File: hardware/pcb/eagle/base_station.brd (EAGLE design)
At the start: 100 x 112 mm, 105 parts, among them CON1 RJ45-8PTH, CON2 RJ45-8PTH, CON3 RJ45-8PTH, CON4 RJ45-8PTH, CON5 RJ45-8PTH, CON6 RJ45-8PTH, CON7 RJ45-8PTH, CON8 RJ45-8PTH, IC1 LTC2851S, IC10 LTC2851S, IC11 LTC2851S, IC12 LTC2851S, IC13 LTC2851S, IC14 LTC2851S, IC15 LTC2851S, IC16 LTC2851S, IC17 NC7WZ16P6X, IC18 7Q-16.368MBG-T, IC19 LTC2851S, IC2 LTC2851S, IC20 LTC2851S, IC21 LTC2851S, IC22 LTC2851S, IC23 LTC2851S, IC24 LTC2851S, IC25 LTC2851S, IC26 LTC2851S, IC3 LTC2851S, IC4 LTC2851S, IC5 LTC2851S, IC6 LTC2851S, IC7 LTC2851S, IC8 LTC2851S, IC9 LTC2851S

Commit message: Changes to oscillator circuit. Added RJ45 for SPI
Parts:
- removed R31: 100k, rcl:R0603
- added CON12: RJ45-8PTH, SparkFun:RJ45-8
- added U$3: WING4, Papilio:WINGSIDE_4BIT
- moved IC17 0.25 mm to (52.8, 39.4)
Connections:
- net N$1 renamed CLK_FPGA
- removed net NC: U$1.A25
- new net MISO: CON12.4, U$3.2
- new net MOSI: CON12.6, U$3.3
- new net N/C: IC17.P$1
- new net SCLK: CON12.8, U$3.4
- new net SS: CON12.3, U$3.1
- new net START: CON12.2, U$1.A25
- net +24V_L: now also CON12.1
- net CLK_OUT: no longer R31.1
- net GND: now also CON12.5, CON12.7
- net N$6: no longer IC17.P$1, R31.2
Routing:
- net +24V_L: track 84.6 -> 133.9 mm
- net CLK_OUT_2: track 44.2 -> 31.4 mm
- net START: track 0.00 -> 9.98 mm, vias 0 -> 1
- net SS: track 0.00 -> 9.46 mm, vias 0 -> 1
- net SCLK: track 0.00 -> 6.39 mm, vias 0 -> 1
- net MOSI: track 0.00 -> 6.39 mm, vias 0 -> 1
- net MISO: track 0.00 -> 6.39 mm, vias 0 -> 1
- net N$6: track 13.9 -> 9.89 mm
- net CLK_OUT: track 169.7 -> 169.1 mm
- net VCC: vias 35 -> 34
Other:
- board size 100 x 112 mm -> 105 x 112 mm

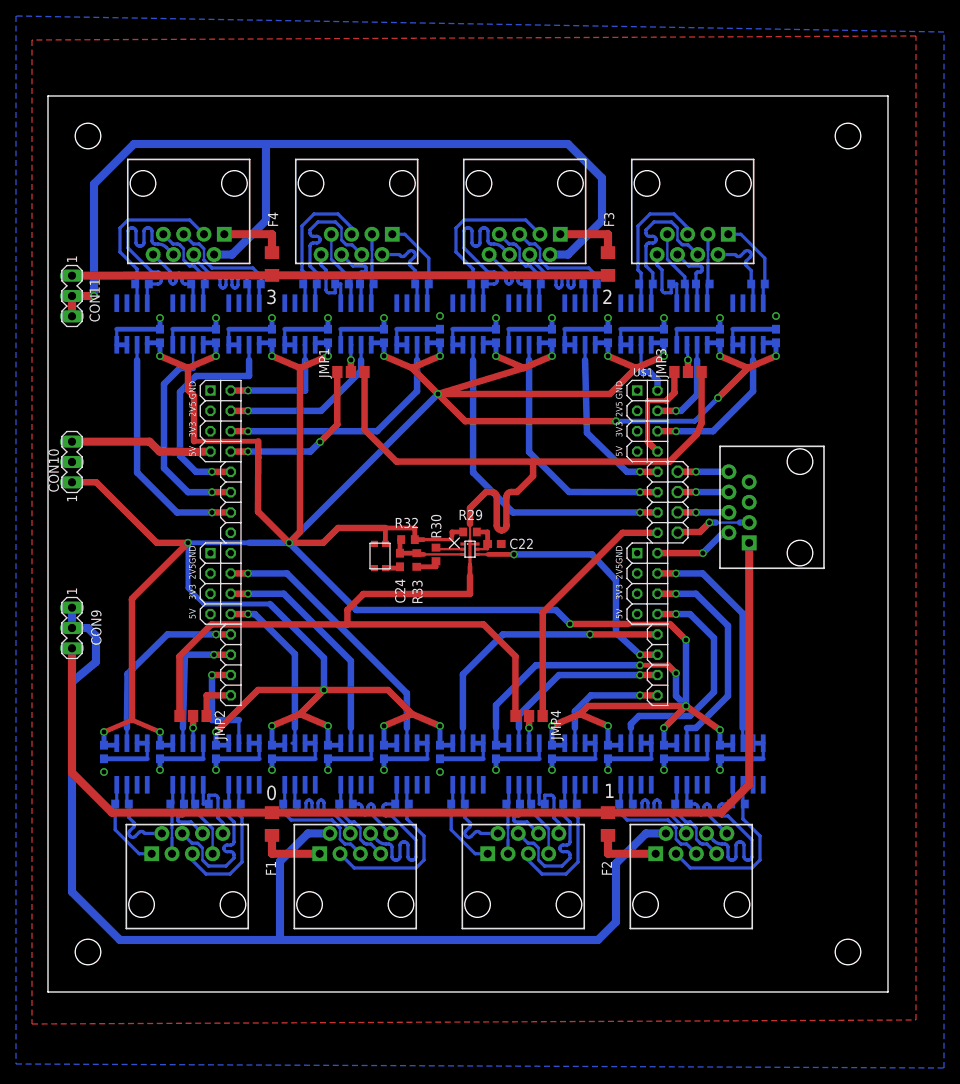
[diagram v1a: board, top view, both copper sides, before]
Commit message: Added silk screen layers, and ammended component names to suit
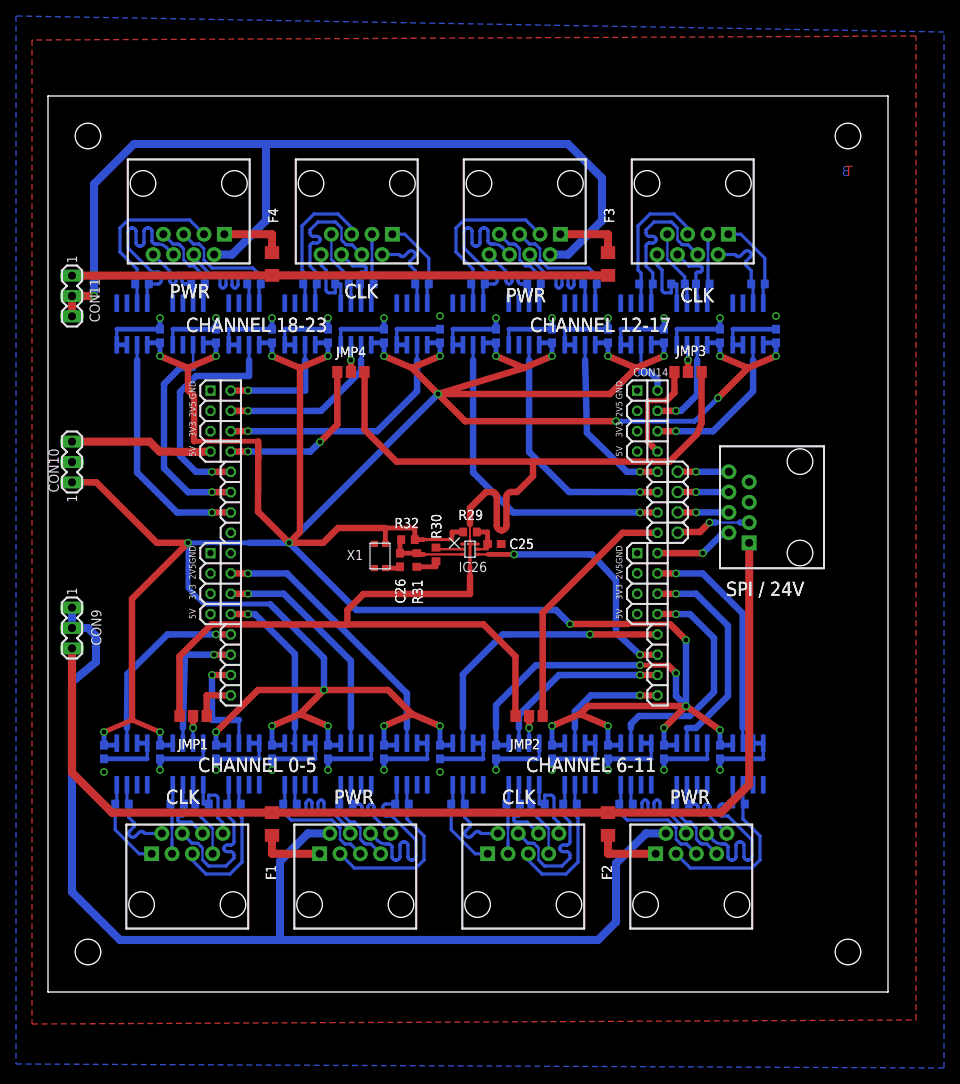
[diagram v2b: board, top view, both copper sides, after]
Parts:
- removed IC25: LTC2851S, texas_lvds:SOIC8
- added X1: 7Q-16.368MBG-T, texas_lvds:4-SMD
- C24: value 2200p -> 0.1uF
- C26: value 0.1uF -> 2200p
- IC17: value NC7WZ16P6X -> LTC2851S; device texas_lvds:NC7WZ16P6X -> texas_lvds:SOIC8
- IC18: value 7Q-16.368MBG-T -> LTC2851S; device texas_lvds:4-SMD -> texas_lvds:SOIC8
- IC26: value LTC2851S -> NC7WZ16P6X; device texas_lvds:SOIC8 -> texas_lvds:NC7WZ16P6X
- moved JMP4 48.4 mm to (37.9, 61.5), turned to 90 degrees
- moved JMP1 47.3 mm to (18.1, 18.5), turned to 270 degrees
- moved C25 43.4 mm to (55.8, 40.0), flipped to the top, turned to 0 degrees
- moved JMP2 42.0 mm to (60.1, 18.5)
- moved C24 41.0 mm to (14.0, 66.0), flipped to the bottom
- moved IC26 39.9 mm to (52.8, 39.4), flipped to the top, turned to 270 degrees
- moved C22 38.1 mm to (28.0, 66.0), flipped to the bottom, turned to 90 degrees
- moved C26 32.2 mm to (44.0, 38.0), flipped to the top
- moved IC18 31.0 mm to (52.5, 67.5), flipped to the bottom, turned to 0 degrees
- moved IC17 28.9 mm to (59.5, 67.5), flipped to the bottom, turned to 0 degrees
- moved IC20 28.0 mm to (38.5, 67.5)
- moved IC23 28.0 mm to (17.5, 67.5)
- moved C10 14.0 mm to (70.0, 14.0)
- moved C12 14.0 mm to (84.0, 14.0)
- moved C13 14.0 mm to (91.0, 66.0)
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- renumbered R33 to R31, U$1 to CON14, U$3 to CON13
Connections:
- net CLK_1: now also JMP1.2; no longer JMP2.2
- net CLK_2: now also JMP2.2; no longer JMP4.2
- net CLK_4: now also IC20.3, JMP4.2; no longer IC22.3, JMP1.2
- net CLK_FPGA: now also IC26.P$4; no longer IC17.P$4
- net CLK_INV_2: now also R10.2; no longer R9.2
- net CLK_INV_3: now also R17.2; no longer R16.2
- net CLK_INV_4: now also IC20.6, R24.2; no longer IC22.6, R23.2
- net CLK_NINV_2: now also R10.1; no longer R9.1
- net CLK_NINV_3: now also R17.1; no longer R16.1
- net CLK_NINV_4: now also IC20.5, R24.1; no longer IC22.5, R23.1
- net CLK_OUT: now also IC26.P$6; no longer IC17.P$6
- net CLK_OUT_1: now also JMP1.1; no longer JMP2.1
- net CLK_OUT_2: now also JMP2.1; no longer JMP4.1
- net CLK_OUT_4: now also JMP4.1; no longer JMP1.1
- net DT_1_4: now also IC20.2; no longer IC22.2
- net DT_1_INV_2: now also R9.1; no longer R10.1
- net DT_1_INV_3: now also R16.1; no longer R17.1
- net DT_1_INV_4: now also IC20.8, R23.1; no longer IC22.8, R24.1
- net DT_1_NINV_2: now also R9.2; no longer R10.2
- net DT_1_NINV_3: now also R16.2; no longer R17.2
- net DT_1_NINV_4: now also IC20.7, R23.2; no longer IC22.7, R24.2
- net DT_2_2: now also IC9.2; no longer IC7.2
- net DT_2_3: now also IC15.2; no longer IC13.2
- net DT_2_INV_2: now also IC9.7, R11.1; no longer IC7.7, R8.1
- net DT_2_INV_3: now also IC15.7, R18.1; no longer IC13.7, R15.1
- net DT_2_INV_4: now also R25.1; no longer R22.1
- net DT_2_NINV_2: now also IC9.8, R11.2; no longer IC7.8, R8.2
- net DT_2_NINV_3: now also IC15.8, R18.2; no longer IC13.8, R15.2
- net DT_2_NINV_4: now also R25.2; no longer R22.2
- net DT_3_2: now also IC7.2; no longer IC9.2
- net DT_3_3: now also IC13.2; no longer IC15.2
- net DT_3_4: now also IC19.2; no longer IC23.2
- net DT_3_INV_2: now also IC7.7, R8.1; no longer IC9.7, R11.1
- net DT_3_INV_3: now also IC13.7, R15.1; no longer IC15.7, R18.1
- net DT_3_INV_4: now also IC19.7, R22.1; no longer IC23.7, R25.1
- net DT_3_NINV_2: now also IC7.8, R8.2; no longer IC9.8, R11.2
- net DT_3_NINV_3: now also IC13.8, R15.2; no longer IC15.8, R18.2
- net DT_3_NINV_4: now also IC19.8, R22.2; no longer IC23.8, R25.2
- net DT_4_3: now also IC17.2; no longer IC19.2
- net DT_4_4: now also IC23.2; no longer IC25.2
- net DT_4_INV_3: now also IC17.7; no longer IC19.7
- net DT_4_INV_4: now also IC23.7; no longer IC25.7
- net DT_4_NINV_3: now also IC17.8; no longer IC19.8
- net DT_4_NINV_4: now also IC23.8; no longer IC25.8
- net DT_5_2: now also IC12.2; no longer IC10.2
- net DT_5_3: now also IC18.2; no longer IC16.2
- net DT_5_INV_2: now also IC12.7, R14.1; no longer IC10.7, R12.1
- net DT_5_INV_3: now also IC18.7, R21.1; no longer IC16.7, R19.1
- net DT_5_INV_4: now also R28.1; no longer R26.1
- net DT_5_NINV_2: now also IC12.8, R14.2; no longer IC10.8, R12.2
- net DT_5_NINV_3: now also IC18.8, R21.2; no longer IC16.8, R19.2
- net DT_5_NINV_4: now also R28.2; no longer R26.2
- net DT_6_2: now also IC10.2; no longer IC12.2
- net DT_6_3: now also IC16.2; no longer IC20.2
- net DT_6_4: now also IC22.2; no longer IC26.2
- net DT_6_INV_2: now also IC10.7, R12.1; no longer IC12.7, R14.1
- net DT_6_INV_3: now also IC16.7, R19.1; no longer IC20.7, R21.1
- net DT_6_INV_4: now also IC22.7, R26.1; no longer IC26.7, R28.1
- net DT_6_NINV_2: now also IC10.8, R12.2; no longer IC12.8, R14.2
- net DT_6_NINV_3: now also IC16.8, R19.2; no longer IC20.8, R21.2
- net DT_6_NINV_4: now also IC22.8, R26.2; no longer IC26.8, R28.2
- net GND: now also C24.2, IC17.4, IC18.3, IC18.4, IC19.3, IC22.3, X1.PAD_1, X1.PAD_2; no longer C26.2, IC18.PAD_1, IC18.PAD_2, IC20.3, IC23.3, IC25.4, IC26.3, IC26.4
- net N$4: now also IC26.P$2; no longer IC17.P$2
- net N$5: now also C25.1, IC26.P$5; no longer C22.1, IC17.P$5
- net N$6: now also C26.2, IC26.P$3; no longer C24.2, IC17.P$3
- net N$9: now also C26.1, X1.PAD_3; no longer C24.1, IC18.PAD_3
- net N/C: now also IC26.P$1; no longer IC17.P$1
- net VCC: now also C22.1, C24.1, IC17.1, IC18.1, X1.PAD_4; no longer C25.1, C26.1, IC18.PAD_4, IC25.1, IC26.1
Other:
- board text added: "B"
- board text added: "C1"
- board text added: "C10"
- board text added: "C11"
- board text added: "C12"
- board text added: "C13"
- board text added: "C14"
- board text added: "C15"
- board text added: "C16"
- board text added: "C17"
- board text added: "C18"
- board text added: "C19"
- board text added: "C2"
- board text added: "C20"
- board text added: "C21"
- board text added: "C22"
- board text added: "C23"
- board text added: "C24"
- board text added: "C25"
- board text added: "C26"
- board text added: "C3"
- board text added: "C4"
- board text added: "C5"
- board text added: "C6"
- board text added: "C7"
- board text added: "C8"
- board text added: "C9"
- board text added: "CHANNEL 0-5"
- board text added: "CHANNEL 12-17"
- board text added: "CHANNEL 18-23"
- board text added: "CHANNEL 6-11"
- board text added: "CLK"
- board text added: "F1"
- board text added: "F2"
- board text added: "F3"
- board text added: "F4"
- board text added: "IC1"
- board text added: "IC10"
- board text added: "IC11"
- board text added: "IC12"
- board text added: "IC13"
- board text added: "IC14"
- board text added: "IC15"
- board text added: "IC16"
- board text added: "IC17"
- board text added: "IC18"
- board text added: "IC19"
- board text added: "IC2"
- board text added: "IC20"
- board text added: "IC21"
- board text added: "IC22"
- board text added: "IC23"
- board text added: "IC24"
- board text added: "IC26"
- board text added: "IC3"
- board text added: "IC4"
- board text added: "IC5"
- board text added: "IC6"
- board text added: "IC7"
- board text added: "IC8"
- board text added: "IC9"
- board text added: "JMP1"
- board text added: "JMP2"
- board text added: "JMP3"
- board text added: "JMP4"
- board text added: "PWR"
- board text added: "R1"
- board text added: "R10"
- board text added: "R11"
- board text added: "R12"
- board text added: "R13"
- board text added: "R14"
- board text added: "R15"
- board text added: "R16"
- board text added: "R17"
- board text added: "R18"
- board text added: "R19"
- board text added: "R2"
- board text added: "R20"
- board text added: "R21"
- board text added: "R22"
- board text added: "R23"
- board text added: "R24"
- board text added: "R25"
- board text added: "R26"
- board text added: "R27"
- board text added: "R28"
- board text added: "R29"
- board text added: "R3"
- board text added: "R30"
- board text added: "R31"
- board text added: "R32"
- board text added: "R4"
- board text added: "R5"
- board text added: "R6"
- board text added: "R7"
- board text added: "R8"
- board text added: "R9"
- board text added: "SPI / 24V"
- board text added: "T"
- board text added: "X1"
- board text removed: "0"
- board text removed: "1"
- board text removed: "2"
- board text removed: "3"
